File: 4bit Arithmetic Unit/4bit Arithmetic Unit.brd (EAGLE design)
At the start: 161.3 x 108.9 mm, 100 parts

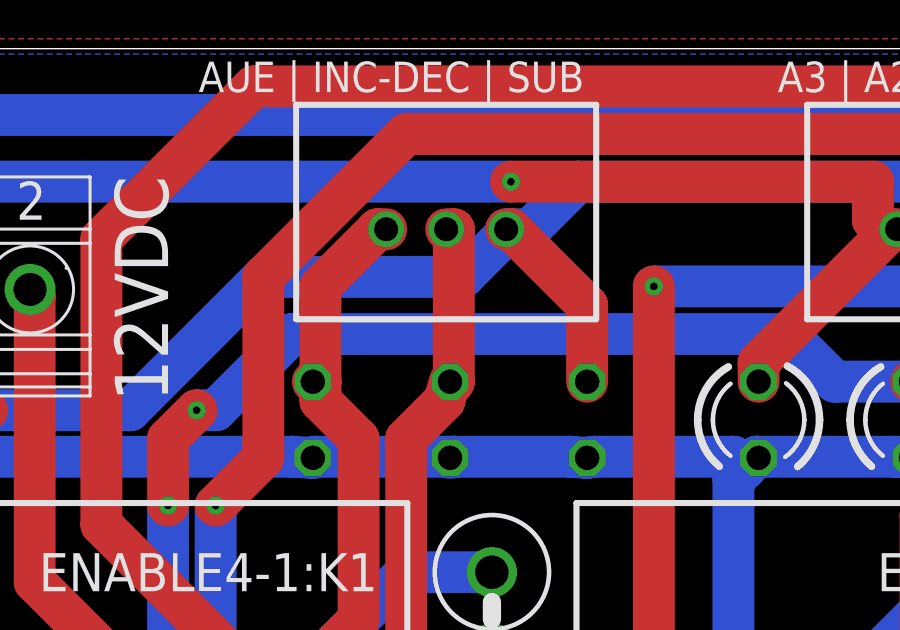
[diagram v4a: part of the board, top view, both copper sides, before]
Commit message: The AU opcode wires were switched
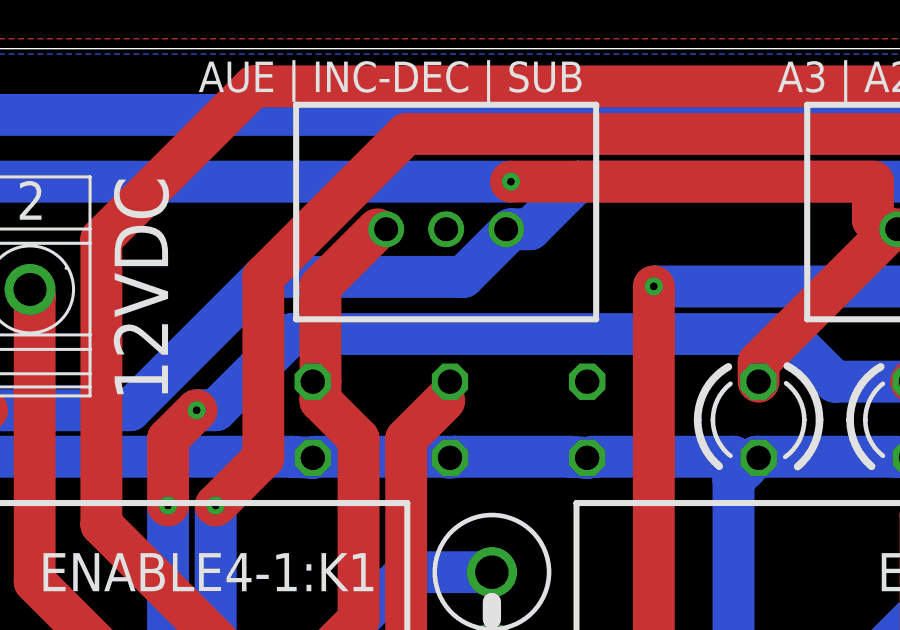
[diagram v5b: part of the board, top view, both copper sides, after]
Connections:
- new net INPUT3-1:IN1: INPUT3-1:LED1.A, INPUT3-1:X1.2
- net INC/DEC: now also INPUT3-1:LED0.A, INPUT3-1:X1.3; no longer INPUT3-1:LED1.A, INPUT3-1:X1.2
- net SUB: no longer INPUT3-1:LED0.A, INPUT3-1:X1.3
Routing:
- net SUB: track 204.9 -> 198.5 mm
- net INC/DEC: track 97.3 -> 91.2 mm
- net AUE: track 272.4 -> 271.8 mm
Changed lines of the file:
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@@
 <?xml version="1.0" encoding="utf-8"?>
 <!DOCTYPE eagle SYSTEM "eagle.dtd">
-<eagle version="8.3.2">
+<eagle version="8.7.0">
 <drawing>
 <settings>
@@
 <param name="dpMaxLengthDifference" value="10mm"/>
 <param name="dpGapFactor" value="2.5"/>
-<param name="checkGrid" value="0"/>
 <param name="checkAngle" value="0"/>
 <param name="checkFont" value="1"/>
 <param name="checkRestrict" value="1"/>
+<param name="checkStop" value="0"/>
+<param name="checkValues" value="0"/>
 <param name="useDiameter" value="13"/>
 <param name="maxErrors" value="50"/>
@@
 <contactref element="ENABLE4-3:D1" pad="C"/>
 <contactref element="ENABLE4-4:D1" pad="C"/>
-<contactref element="INPUT3-1:LED2" pad="A"/>
-<contactref element="INPUT3-1:X1" pad="1"/>
 <wire x1="20.32" y1="100.965" x2="22.225" y2="102.87" width="1.397" layer="1"/>
 <wire x1="20.32" y1="97.79" x2="20.32" y2="100.965" width="1.397" layer="1"/>
-<wire x1="22.225" y1="102.87" x2="22.511" y2="102.87" width="1.397" layer="1"/>
-<wire x1="20.32" y1="97.79" x2="20.066" y2="97.79" width="1.397" layer="1"/>
 <wire x1="23.1775" y1="91.44" x2="26.035" y2="91.44" width="1.397" layer="16"/>
 <wire x1="18.7325" y1="86.995" x2="23.1775" y2="91.44" width="1.397" layer="16"/>
@@
 <wire x1="18.415" y1="87.63" x2="18.665" y2="86.995" width="1.397" layer="1"/>
 <wire x1="74.295" y1="98.7425" x2="74.77125" y2="98.26625" width="1.397" layer="1"/>
+<contactref element="INPUT3-1:LED2" pad="A"/>
+<contactref element="INPUT3-1:X1" pad="1"/>
+<wire x1="22.225" y1="102.87" x2="22.511" y2="102.87" width="0" layer="19" extent="1-1"/>
+<wire x1="20.066" y1="97.79" x2="20.32" y2="97.79" width="0" layer="19" extent="1-1"/>
 </signal>
 <signal name="INC/DEC">
-<contactref element="INPUT3-1:LED1" pad="A"/>
-<contactref element="INPUT3-1:X1" pad="2"/>
 <contactref element="INC/DEC_FILTER1:K1" pad="A2"/>
 <contactref element="INC/DEC_FILTER1:D1" pad="C"/>
-<wire x1="24.765" y1="97.79" x2="24.765" y2="102.87" width="1.397" layer="1"/>
-<wire x1="24.765" y1="102.87" x2="24.511" y2="102.87" width="1.397" layer="1"/>
-<wire x1="24.765" y1="97.79" x2="24.638" y2="97.79" width="1.397" layer="1"/>
 <wire x1="74.6125" y1="95.5675" x2="75.565" y2="96.52" width="1.397" layer="1"/>
 <wire x1="74.6125" y1="86.995" x2="74.6125" y2="95.5675" width="1.397" layer="1"/>
@@
 <wire x1="65.0875" y1="86.995" x2="55.88" y2="77.7875" width="1.397" layer="16"/>
 <wire x1="74.545" y1="86.995" x2="65.0875" y2="86.995" width="1.397" layer="16"/>
-<wire x1="24.4475" y1="97.155" x2="24.638" y2="97.79" width="1.397" layer="1"/>
 <via x="55.88" y="77.7875" extent="1-16" drill="0.254"/>
+<contactref element="INPUT3-1:LED0" pad="A"/>
+<contactref element="INPUT3-1:X1" pad="3"/>
+<wire x1="29.21" y1="97.79" x2="26.511" y2="102.87" width="0" layer="19" extent="1-1"/>
+<wire x1="24.4475" y1="97.155" x2="29.21" y2="97.79" width="0" layer="19" extent="1-1"/>
 </signal>
 <signal name="SUB">
@@
 <contactref element="ADDER8-1:D1" pad="C"/>
 <contactref element="ADDER8-1:K1" pad="1"/>
-<contactref element="INPUT3-1:LED0" pad="A"/>
-<contactref element="INPUT3-1:X1" pad="3"/>
 <wire x1="100.0125" y1="95.5675" x2="100.965" y2="96.52" width="1.397" layer="1"/>
 <wire x1="100.0125" y1="86.995" x2="100.0125" y2="95.5675" width="1.397" layer="1"/>
@@
 <wire x1="5.08" y1="11.43" x2="5.08" y2="15.875" width="1.397" layer="1"/>
 <wire x1="5.08" y1="15.875" x2="5.15" y2="16.14" width="1.397" layer="1"/>
-<wire x1="29.21" y1="100.33" x2="26.67" y2="102.87" width="1.397" layer="1"/>
-<wire x1="29.21" y1="97.79" x2="29.21" y2="100.33" width="1.397" layer="1"/>
-<wire x1="26.67" y1="102.87" x2="26.511" y2="102.87" width="1.397" layer="1"/>
 <wire x1="1.27" y1="20.6375" x2="5.08" y2="16.8275" width="1.397" layer="1"/>
 <wire x1="1.27" y1="88.9" x2="1.27" y2="20.6375" width="1.397" layer="1"/>
@@
 <wire x1="26.67" y1="102.87" x2="25.0825" y2="101.2825" width="1.397" layer="16"/>
 <wire x1="5.08" y1="16.8275" x2="5.15" y2="16.14" width="1.397" layer="1"/>
-<wire x1="26.67" y1="102.87" x2="26.511" y2="102.87" width="1.397" layer="16"/>
 <wire x1="93.0275" y1="104.4575" x2="100.965" y2="96.52" width="1.397" layer="16"/>
 <wire x1="28.8925" y1="104.4575" x2="93.0275" y2="104.4575" width="1.397" layer="16"/>
@@
 <wire x1="137.795" y1="17.78" x2="138.27125" y2="17.30375" width="1.397" layer="1"/>
 </signal>
+<signal name="INPUT3-1:IN1">
+<contactref element="INPUT3-1:LED1" pad="A"/>
+<contactref element="INPUT3-1:X1" pad="2"/>
+<wire x1="24.638" y1="97.79" x2="24.511" y2="102.87" width="0" layer="19" extent="1-1"/>
+</signal>
 </signals>

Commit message: Fixing AU subtraction CARRY bug
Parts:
- removed ADDER8-1:D5: 1N4007, relay_computer_custom:RAD2,5
- removed ADDER8-1:D6: 1N5359, relay_computer_custom:C1702-05
- removed ADDER8-1:K3: HF41F-12-Z, relay_computer_custom:HF41F-12-Z
- ADDER8-1:ADDER1-0:D2, ADDER8-1:ADDER1-0:D4, ADDER8-1:ADDER1-1:D2, ADDER8-1:ADDER1-1:D4, ADDER8-1:ADDER1-2:D2, ADDER8-1:ADDER1-2:D4, ADDER8-1:ADDER1-3:D2, ADDER8-1:ADDER1-3:D4, ADDER8-1:D2, ADDER8-1:D4, ENABLE4-1:D2, ENABLE4-2:D2, ENABLE4-3:D2, ENABLE4-4:D2, INC/DEC_FILTER1:D2, SUB_XOR1:D10, SUB_XOR1:D2, SUB_XOR1:D4, SUB_XOR1:D6, SUB_XOR1:D8, ZERO_DETECT1:D2, ZERO_DETECT1:D4, ZERO_DETECT1:D6, ZERO_DETECT1:D8: value 1N5359 -> 1N5359VERT_SML; device relay_computer_custom:C1702-05 -> relay_computer_custom:RAD2.5_D2
- ADDER8-1:K2: value HF41F-12-Z -> PY14-02; device relay_computer_custom:HF41F-12-Z -> relay_computer_custom:PY14-02
- moved ZERO_DETECT1:D8 1301.8 mm to (-1.27, -1235.7), turned to 0 degrees
- moved ZERO_DETECT1:D7 1287.6 mm to (-1.27, -1223.0), turned to 0 degrees
- moved ADDER8-1:D2 1268.1 mm to (-1.27, -1261.1), turned to 0 degrees
- moved ZERO_DETECT1:D6 1267.7 mm to (-1.27, -1210.3), turned to 0 degrees
- moved ADDER8-1:D1 1259.8 mm to (-1.27, -1248.4), turned to 0 degrees
- moved ZERO_DETECT1:D5 1254.1 mm to (-1.27, -1197.6), turned to 0 degrees
- moved ZERO_DETECT1:D4 1248.7 mm to (-1.27, -1184.9), turned to 0 degrees
- moved ZERO_DETECT1:D3 1234.4 mm to (-1.27, -1172.2), turned to 0 degrees
- moved ZERO_DETECT1:D2 1213.9 mm to (-1.27, -1159.5), turned to 0 degrees
- moved ZERO_DETECT1:D1 1200.8 mm to (-1.27, -1146.8), turned to 0 degrees
- moved ADDER8-1:ADDER1-3:D4 1172.7 mm to (-1.27, -1134.1), turned to 0 degrees
- moved ADDER8-1:ADDER1-2:D4 1157.2 mm to (-1.27, -1121.4), turned to 0 degrees
- moved ADDER8-1:ADDER1-1:D4 1142.7 mm to (-1.27, -1108.7), turned to 0 degrees
- moved ADDER8-1:ADDER1-3:D3 1128.5 mm to (-1.27, -1083.3), turned to 0 degrees
- moved ADDER8-1:ADDER1-0:D4 1128.4 mm to (-1.27, -1096.0), turned to 0 degrees
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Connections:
- removed net ADDER8-1:D$3: ADDER8-1:D5.A, ADDER8-1:D6.A
- removed net ADDER8-1:N$10: ADDER8-1:K2.3, ADDER8-1:K3.5
- removed net ADDER8-1:N$11: ADDER8-1:K2.5, ADDER8-1:K3.3
- new net ADDER8-1:IN: ADDER8-1:D3.C, ADDER8-1:K2.A2
- new net ADDER8-1:N$5: ADDER8-1:ADDER1-3:K2.11
- net +12V: no longer ADDER8-1:K2.4
- net ADDER8-1:IN1: now also ADDER8-1:K2.42; no longer ADDER8-1:D3.C, ADDER8-1:K2.1
- net ADDER8-1:N$6: now also ADDER8-1:K2.44
- net ADDER8-1:N$7: now also ADDER8-1:K2.34
- net ADDER8-1:N$9: now also ADDER8-1:K2.32
- net GND: now also ADDER8-1:K2.A1; no longer ADDER8-1:D6.C, ADDER8-1:K2.2, ADDER8-1:K3.2
- net N$25: now also ADDER8-1:K2.31; no longer ADDER8-1:ADDER1-3:K2.11, ADDER8-1:D5.C, ADDER8-1:K3.1
- net N$44: now also ADDER8-1:K2.41; no longer ADDER8-1:K3.4
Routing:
- net GND: track 722.6 -> 32911.5 mm
- net ZERO_DETECT1:GND: track 94.2 -> 13538.8 mm
- net AUE: track 271.8 -> 5914.0 mm
- net SUB: track 198.5 -> 4675.2 mm
- net N$41: track 157.9 -> 4000.8 mm
- net +12V: track 318.5 -> 3472.0 mm
- net N$40: track 251.7 -> 2961.5 mm
- net ZERO_DETECT1:D$4: track 4.45 -> 2584.4 mm
- net ADDER8-1:D$1: track 4.71 -> 2531.1 mm
- net N$42: track 221.6 -> 2724.7 mm
- net ZERO_DETECT1:D$2: track 4.45 -> 2478.3 mm
- net ZERO_DETECT1:D$1: track 4.45 -> 2411.1 mm
- net N$43: track 125.4 -> 2507.7 mm
- net N$15: track 220.4 -> 2437.1 mm
- net N$14: track 73.1 -> 2260.5 mm
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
